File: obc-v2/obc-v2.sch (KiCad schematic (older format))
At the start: 19 parts

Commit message: obc-v2: Add voltage input and screw terminal
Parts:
- added J?: Screw_Terminal_01x02, symbol Connector:Screw_Terminal_01x02
- C? (x10): symbol Device:C -> obc-v2-rescue:C-Device
- FB?: symbol Device:Ferrite_Bead -> obc-v2-rescue:Ferrite_Bead-Device
- SW?: symbol Switch:SW_Push_Dual -> obc-v2-rescue:SW_Push_Dual-Switch
- U?: symbol MCU_Microchip_SAML_NEW:ATSAML10E16A-AF -> obc-v2-rescue:ATSAML10E16A-AF-MCU_Microchip_SAML_NEW
- U?: symbol Memory_EEPROM:AT25xxx -> obc-v2-rescue:AT25xxx-Memory_EEPROM
- U?: symbol Sensor_Pressure:MS5607-02BA -> obc-v2-rescue:MS5607-02BA-Sensor_Pressure
- U?: symbol Regulator_Linear:MIC5219-3.3YM5 -> obc-v2-rescue:MIC5219-3.3YM5-Regulator_Linear
- X?: symbol Oscillator:ASCO -> obc-v2-rescue:ASCO-Oscillator
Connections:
- net labels added: VIN
- wire segments 54 -> 55
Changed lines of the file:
@@
 RX
 $Comp
-L power:+3.3V #PWR?
+L obc-v2-rescue:+3.3V-power #PWR?
 U 1 1 61149F54
 P 2600 1150
@@
 $EndComp
 $Comp
-L Device:C C?
+L obc-v2-rescue:C-Device C?
 U 1 1 6114B5C3
 P 2300 1750
@@
 $EndComp
 $Comp
-L Device:C C?
+L obc-v2-rescue:C-Device C?
 U 1 1 6114F91D
 P 2300 2000
@@
 	2600 2000 2600 2250
 $Comp
-L power:GND #PWR?
+L obc-v2-rescue:GND-power #PWR?
 U 1 1 61151116
 P 1850 2000
@@
 $EndComp
 $Comp
-L Device:C C?
+L obc-v2-rescue:C-Device C?
 U 1 1 61151D34
 P 3550 2100
@@
 $EndComp
 $Comp
-L power:GND #PWR?
+L obc-v2-rescue:GND-power #PWR?
 U 1 1 611522C8
 P 3150 1550
@@
 $EndComp
 $Comp
-L Device:C C?
+L obc-v2-rescue:C-Device C?
 U 1 1 61159BEC
 P 3000 1700
@@
 $EndComp
 $Comp
-L power:GND #PWR?
+L obc-v2-rescue:GND-power #PWR?
 U 1 1 61107CFD
 P 2900 4350
@@
 $EndComp
 $Comp
-L Device:C C?
+L obc-v2-rescue:C-Device C?
 U 1 1 6115BCFD
 P 3000 1900
@@
 	2850 1700 2700 1700
 $Comp
-L Device:C C?
+L obc-v2-rescue:C-Device C?
 U 1 1 61165FAE
 P 3550 1150
@@
 	2150 1750 1850 1750
 $Comp
-L Oscillator:ASCO X?
+L obc-v2-rescue:ASCO-Oscillator X?
 U 1 1 611689B2
 P 5350 1350
@@
 $EndComp
 $Comp
-L power:GND #PWR?
+L obc-v2-rescue:GND-power #PWR?
 U 1 1 6116B41C
 P 5350 1650
@@
 $EndComp
 $Comp
-L power:+3.3V #PWR?
+L obc-v2-rescue:+3.3V-power #PWR?
 U 1 1 6116B9D5
 P 5350 1050
@@
 32-bit 32MHz ARM Processor
 $Comp
-L Memory_EEPROM:AT25xxx U?
+L obc-v2-rescue:AT25xxx-Memory_EEPROM U?
 U 1 1 61172006
 P 5500 2750
@@
 $EndComp
 $Comp
-L power:GND #PWR?
+L obc-v2-rescue:GND-power #PWR?
 U 1 1 611762E7
 P 5500 3050
@@
 $EndComp
 $Comp
-L power:+3.3V #PWR?
+L obc-v2-rescue:+3.3V-power #PWR?
 U 1 1 611767CC
 P 5500 2450
@@
 SCK
 $Comp
-L power:+3.3V #PWR?
+L obc-v2-rescue:+3.3V-power #PWR?
 U 1 1 611772E8
 P 5000 2650
@@
 4MB Flash Memory
 $Comp
-L Device:Ferrite_Bead FB?
+L obc-v2-rescue:Ferrite_Bead-Device FB?
 U 1 1 611AF1D7
 P 2600 1550
@@
 	3700 2100 3700 1150
 $Comp
-L power:GND #PWR?
+L obc-v2-rescue:GND-power #PWR?
 U 1 1 611FC866
 P 3700 1050
@@
 NoConn ~ 7450 3700
 $Comp
-L power:GND #PWR?
+L obc-v2-rescue:GND-power #PWR?
 U 1 1 612718CF
 P 7550 4200
@@
 	7850 4200 7950 4200
 $Comp
-L power:+3V3 #PWR?
+L obc-v2-rescue:+3V3-power #PWR?
 U 1 1 61272ED0
 P 7300 3600
@@
 INT4_GYRO
 $Comp
-L power:+3V3 #PWR?
+L obc-v2-rescue:+3V3-power #PWR?
 U 1 1 61277D25
 P 7600 2550
@@
 $EndComp
 $Comp
-L power:+3V3 #PWR?
+L obc-v2-rescue:+3V3-power #PWR?
 U 1 1 612781FE
 P 8100 2550
@@
 $EndComp
 $Comp
-L Device:C C?
+L obc-v2-rescue:C-Device C?
 U 1 1 612799A4
 P 7600 2700
@@
 $EndComp
 $Comp
-L Device:C C?
+L obc-v2-rescue:C-Device C?
 U 1 1 6127A006
 P 8100 2700
@@
 $EndComp
 $Comp
-L power:GND #PWR?
+L obc-v2-rescue:GND-power #PWR?
 U 1 1 6127AE14
 P 7600 2850
@@
 $EndComp
 $Comp
-L power:GND #PWR?
+L obc-v2-rescue:GND-power #PWR?
 U 1 1 6127B677
 P 8100 2850
@@
 INT4_GYRO
 $Comp
-L MCU_Microchip_SAML_NEW:ATSAML10E16A-AF U?
+L obc-v2-rescue:ATSAML10E16A-AF-MCU_Microchip_SAML_NEW U?
 U 1 1 61106D2F
 P 2750 3250
@@
 	6900 2250 9050 2250
 $Comp
-L Sensor_Pressure:MS5607-02BA U?
+L obc-v2-rescue:MS5607-02BA-Sensor_Pressure U?
 U 1 1 61291CE6
 P 9100 1400
@@
 $EndComp
 $Comp
-L power:GND #PWR?
+L obc-v2-rescue:GND-power #PWR?
 U 1 1 61292644
 P 9100 1800
@@
 $EndComp
 $Comp
-L power:+3V3 #PWR?
+L obc-v2-rescue:+3V3-power #PWR?
 U 1 1 61292BCA
 P 9100 1000
@@
 $EndComp
 $Comp
-L power:GND #PWR?
+L obc-v2-rescue:GND-power #PWR?
 U 1 1 6129E849
 P 5400 4700
@@
 $EndComp
 $Comp
-L power:+3V3 #PWR?
+L obc-v2-rescue:+3V3-power #PWR?
 U 1 1 6129EE3F
 P 5400 4050
@@
 1-wire Interface
 $Comp
-L Switch:SW_Push_Dual SW?
+L obc-v2-rescue:SW_Push_Dual-Switch SW?
 U 1 1 612A144F
 P 1600 1150
@@
 RESET*
 $Comp
-L power:GND #PWR?
+L obc-v2-rescue:GND-power #PWR?
 U 1 1 61309369
 P 1400 1350
@@
 	1800 1150 1800 1350
 $Comp
-L Regulator_Linear:MIC5219-3.3YM5 U?
+L obc-v2-rescue:MIC5219-3.3YM5-Regulator_Linear U?
 U 1 1 6130CF2C
 P 3000 5500
@@
 $EndComp
 $Comp
-L power:GND #PWR?
+L obc-v2-rescue:GND-power #PWR?
 U 1 1 6130E43E
 P 3000 5800
@@
 $EndComp
 $Comp
-L power:+3V3 #PWR?
+L obc-v2-rescue:+3V3-power #PWR?
 U 1 1 6130EAA8
 P 3750 5400
@@
 $EndComp
 $Comp
-L Device:C C?
+L obc-v2-rescue:C-Device C?
 U 1 1 6130FC01
 P 3450 5250
@@
 	3300 5400 3450 5400
 $Comp
-L power:GND #PWR?
+L obc-v2-rescue:GND-power #PWR?
 U 1 1 61312359
 P 3450 5100
@@
 Connection ~ 3450 5400
 $Comp
-L Device:C C?
+L obc-v2-rescue:C-Device C?
 U 1 1 61313A92
 P 3450 5650
@@
 $EndComp
 $Comp
-L power:GND #PWR?
+L obc-v2-rescue:GND-power #PWR?
 U 1 1 613140DB
 P 3450 5800
@@
 	3300 5500 3450 5500
 Wire Notes Line
-	2250 4850 4100 4850
-Wire Notes Line
 	4100 4850 4100 6200
 Wire Notes Line
-	4100 6200 2250 6200
-Wire Notes Line
-	2250 6200 2250 4850
+	1750 6200 1750 4850
 Text Notes 2300 6150 0    50   ~ 0
 Voltage Regulator
+$Comp
+L Connector:Screw_Terminal_01x02 J?
+U 1 1 61396620
+P 1950 5550
+F 0 "J?" H 1900 5650 50  0000 L CNN
+F 1 "Screw_Terminal_01x02" V 2050 5100 50  0000 L CNN
+F 2 "" H 1950 5550 50  0001 C CNN
+F 3 "" H 1950 5550 50  0001 C CNN
+	1    1950 5550
+	-1   0    0    1
+$EndComp
+$Comp
+L obc-v2-rescue:GND-power #PWR?
+U 1 1 6139C9C7
+P 2150 5450
+F 0 "#PWR?" H 2150 5200 50  0001 C CNN
+F 1 "GND" V 2150 5250 50  0000 C CNN
+F 2 "" H 2150 5450 50  0001 C CNN
+F 3 "" H 2150 5450 50  0001 C CNN
+	1    2150 5450
+	0    -1   -1   0
+$EndComp
+Wire Notes Line
+	1750 4850 4100 4850
+Wire Notes Line
+	1750 6200 4100 6200
+Text GLabel 2150 5550 2    50   Input ~ 0
+VIN
+Text GLabel 2700 5400 0    50   Input ~ 0
+VIN
+Wire Wire Line
+	2700 5500 2700 5400
 $EndSCHEMATC

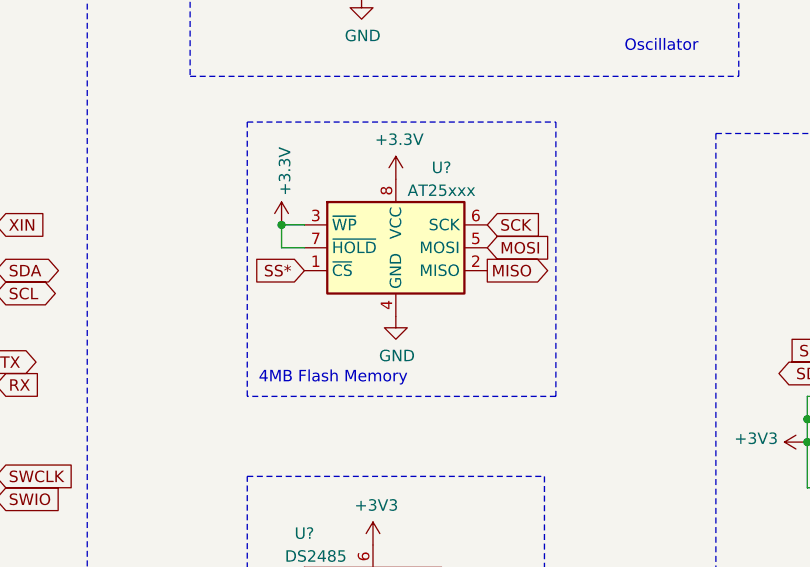
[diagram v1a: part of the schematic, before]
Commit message: obc-v2: Update 4MB flash chip to 1GB
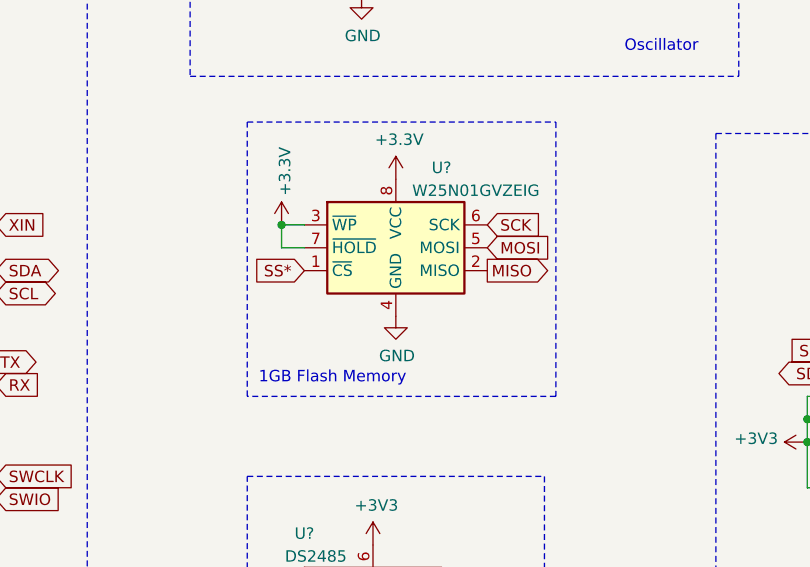
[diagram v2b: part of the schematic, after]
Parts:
- U?: value AT25xxx -> W25N01GVZEIG
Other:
- note added: "1GB Flash Memory"
- note removed: "4MB Flash Memory"
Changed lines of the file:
@@
 P 5500 2750
 F 0 "U?" H 5700 3100 50  0000 C CNN
-F 1 "AT25xxx" H 5700 3000 50  0000 C CNN
+F 1 "W25N01GVZEIG" H 5850 3000 50  0000 C CNN
 F 2 "" H 5500 2750 50  0001 C CNN
 F 3 "http://ww1.microchip.com/downloads/en/DeviceDoc/Atmel-8707-SEEPROM-AT25010B-020B-040B-Datasheet.pdf" H 5500 2750 50  0001 C CNN
@@
 	4850 3400 4850 2200
 Text Notes 4900 3350 0    50   ~ 0
-4MB Flash Memory
+1GB Flash Memory
 $Comp
 L obc-v2-rescue:Ferrite_Bead-Device FB?

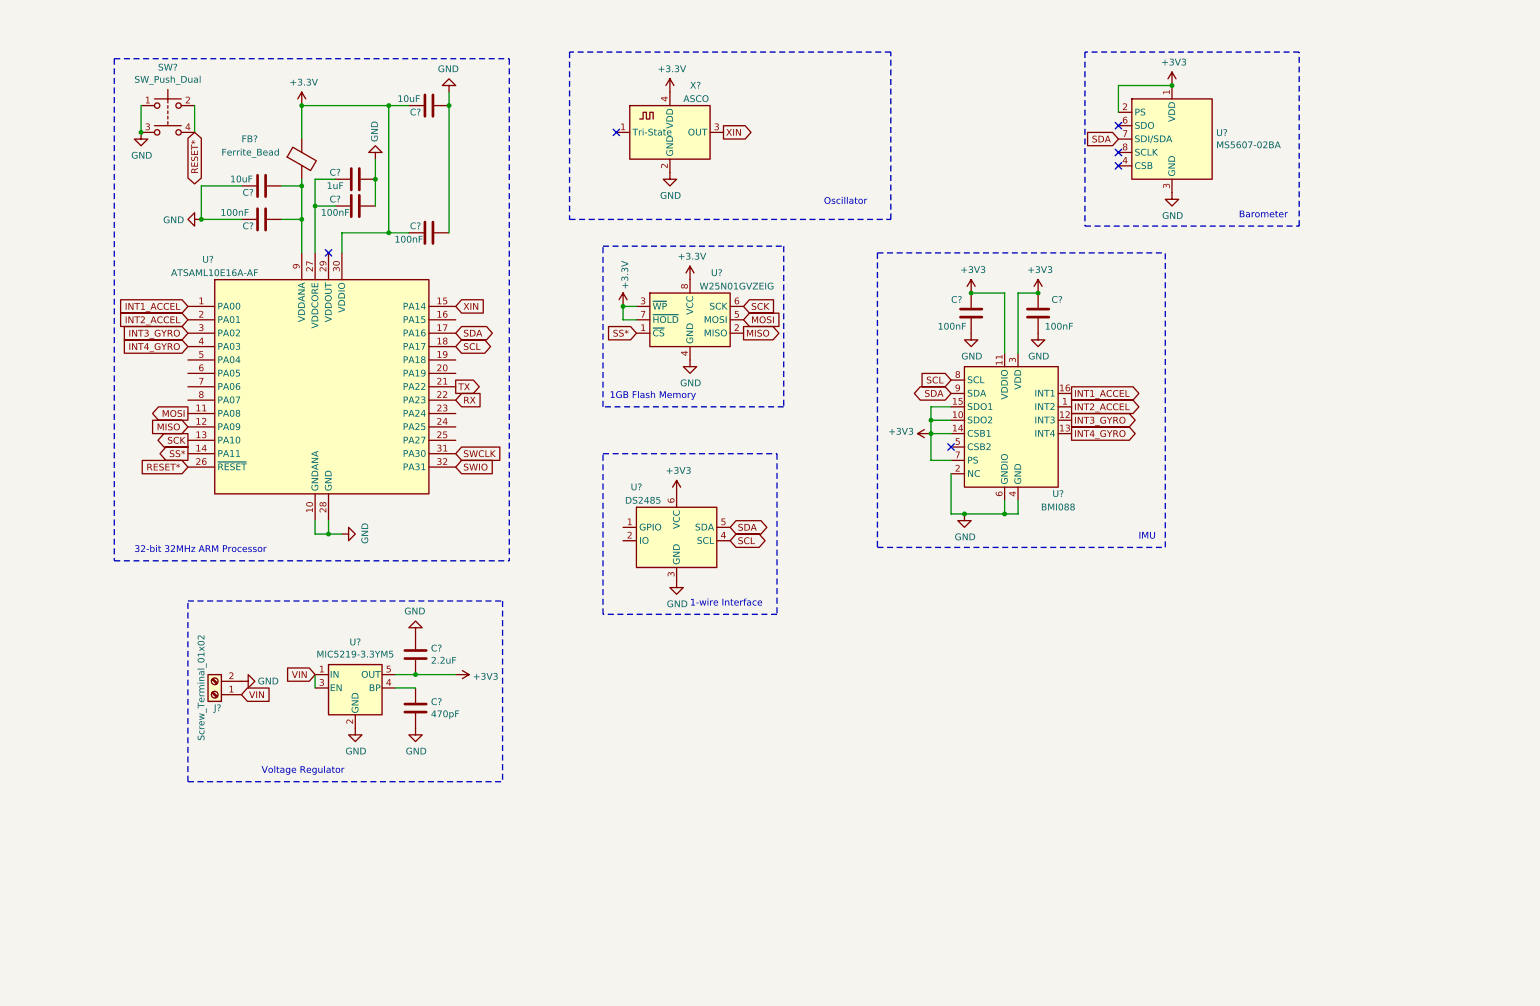
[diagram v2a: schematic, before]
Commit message: obc-v2: Add GPIO connector and LEDs
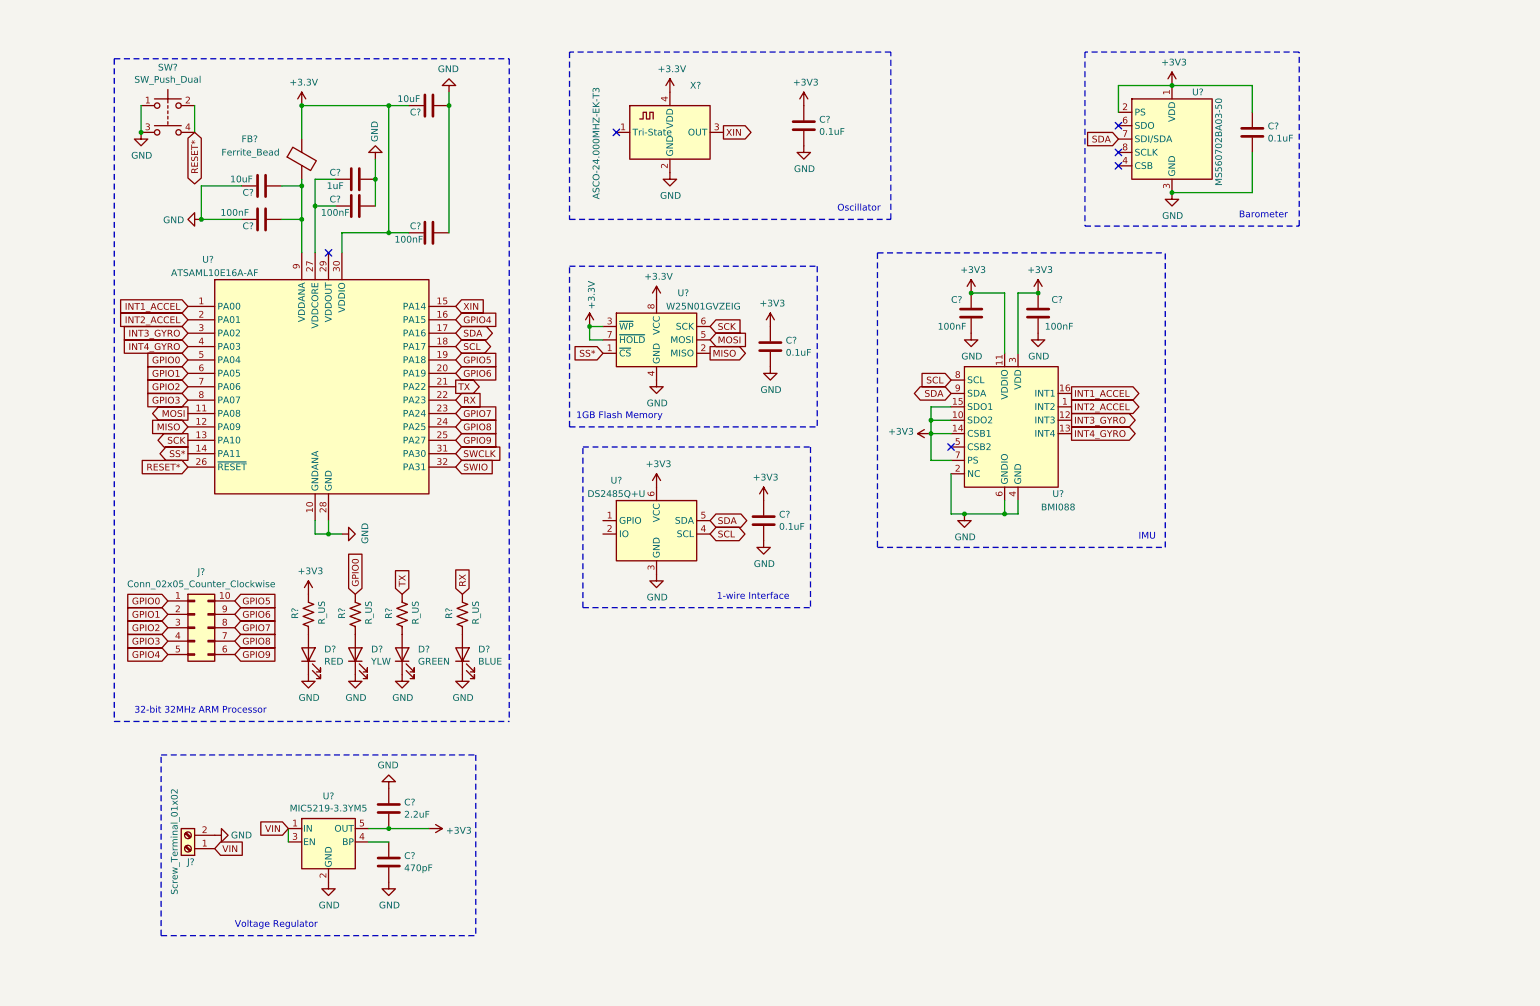
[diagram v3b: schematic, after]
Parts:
- added C? (x4): 0.1uF, symbol Device:C
- added D?: RED, symbol Device:LED
- added D?: YLW, symbol Device:LED
- added D?: GREEN, symbol Device:LED
- added D?: BLUE, symbol Device:LED
- added J?: Conn_02x05_Counter_Clockwise, symbol Connector_Generic:Conn_02x05_Counter_Clockwise
- added R? (x4): R_US, symbol Device:R_US
- U?: value MS5607-02BA -> MS560702BA03-50
- U?: value DS2485 -> DS2485Q+U
- X?: value ASCO -> ASCO-24.000MHZ-EK-T3
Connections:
- net +3V3: now also C?.1, C?.1, C?.1, C?.1, R?.2
- net GND: now also C?.2, C?.2, C?.2, C?.2, D?.1 (K), D?.1 (K), D?.1 (K), D?.1 (K)
- net RX: now also R?.2
- net TX: now also R?.2
- net GPIO4: now reaches U?.16 (PA15)
- net GPIO4: now also J?.5 (Pin_5)
- net GPIO5: now reaches U?.19 (PA18)
- net GPIO5: now also J?.10 (Pin_10)
- net GPIO6: now reaches U?.20 (PA19)
- net GPIO6: now also J?.9 (Pin_9)
- net GPIO7: now reaches U?.23 (PA24)
- net GPIO7: now also J?.8 (Pin_8)
- net GPIO8: now reaches U?.24 (PA25)
- net GPIO8: now also J?.7 (Pin_7)
- net GPIO9: now reaches U?.25 (PA27)
- net GPIO9: now also J?.6 (Pin_6)
- net GPIO0: now reaches U?.5 (PA04)
- net GPIO0: now also J?.1 (Pin_1), R?.2
- net GPIO1: now reaches U?.6 (PA05)
- net GPIO1: now also J?.2 (Pin_2)
- net GPIO2: now reaches U?.7 (PA06)
- net GPIO2: now also J?.3 (Pin_3)
- net GPIO3: now reaches U?.8 (PA07)
- net GPIO3: now also J?.4 (Pin_4)
- new net: D?.2 (A), R?.1 (x4)
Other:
- moved on the sheet: C?, J?, U?

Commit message: obc-v2: Fix reset button. Add debug header, RGB LED, and voltage divider circuit for measurement. Minor fixes to I2C bus, jumpers, and decoupling circuitry
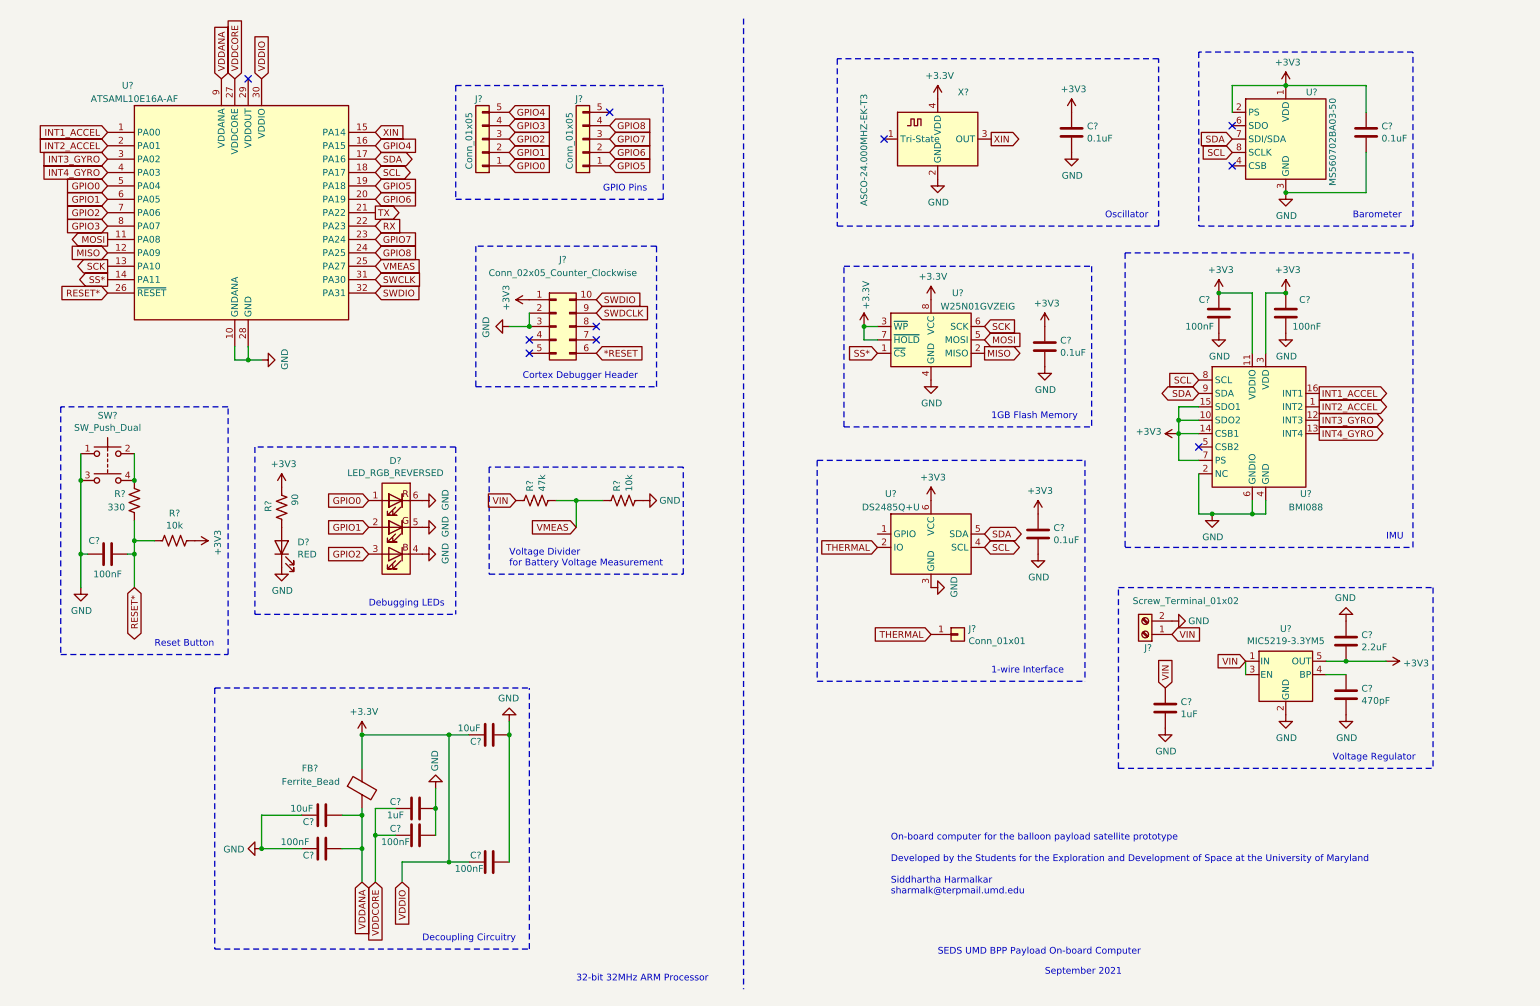
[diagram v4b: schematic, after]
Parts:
- removed D?: YLW, symbol Device:LED
- removed D?: GREEN, symbol Device:LED
- removed D?: BLUE, symbol Device:LED
- removed J?: Conn_02x05_Counter_Clockwise, symbol Connector_Generic:Conn_02x05_Counter_Clockwise
- removed R? (x3): R_US, symbol Device:R_US
- added C?: 100nF, symbol Device:C
- added C?: 1uF, symbol obc-v2-rescue:C-Device
- added D?: LED_RGB_REVERSED, symbol RGB_LED_REVERSED:LED_RGB_REVERSED
- added J? (x2): Conn_01x05, symbol Connector_Generic:Conn_01x05
- added J?: Conn_01x01, symbol Connector_Generic:Conn_01x01
- added J?: Conn_02x05_Counter_Clockwise, symbol Connector_Generic:Conn_02x05_Counter_Clockwise
- added R? (x2): 10k, symbol Device:R_US
- added R?: 330, symbol Device:R_US
- added R?: 47k, symbol Device:R_US
- R?: value R_US -> 90
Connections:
- net +3V3: now also J?.1 (Pin_1), R?.1
- net GND: now also C?.2, C?.2, D?.4 (BA), D?.5 (GA), D?.6 (RA), J?.2 (Pin_2), J?.3 (Pin_3), R?.2
- net GPIO0: now also D?.1 (RK), J?.1 (Pin_1)
- net GPIO1: now also D?.2 (GK), J?.2 (Pin_2)
- net GPIO2: now also D?.3 (BK), J?.3 (Pin_3)
- net GPIO3: now also J?.4 (Pin_4)
- net GPIO4: now also J?.5 (Pin_5)
- net GPIO5: now also J?.1 (Pin_1)
- net GPIO6: now also J?.2 (Pin_2)
- net GPIO7: now also J?.3 (Pin_3)
- net GPIO8: now also J?.4 (Pin_4)
- net RESET*: now also C?.1, R?.2, R?.2; no longer SW?.2, SW?.4
- net SCL: now also U?.8 (SCLK)
- net VIN: now also C?.1, R?.1
- net VDDCORE: now reaches C?.1, C?.1, U?.27 (VDDCORE)
- net VDDANA: now reaches C?.1, C?.2, FB?.2, U?.9 (VDDANA)
- net THERMAL: now reaches U?.2 (IO)
- net THERMAL: now also J?.1 (Pin_1)
- net GPIO9 renamed VMEAS
- net VMEAS: now also R?.1, R?.2
- net SWIO renamed SWDIO
- net SWDIO: now also J?.10 (Pin_10)
- new net: R?.1, SW?.2, SW?.4
- new net *RESET: J?.6 (Pin_6)
- new net SWDCLK: J?.9 (Pin_9)
- no-connect marks 6 -> 10
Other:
- note added: "Cortex Debugger Header"
- note added: "Debugging LEDs"
- note added: "Decoupling Circuitry"
- note added: "GPIO Pins"
- note added: "On-board computer for the balloon payload satellite prototype\n\nDeveloped by the Students for the Exploration and Development of Space at the University of Maryland\n\nSiddhartha Harmalkar\nsharmalk@terpmail.umd.edu"
- note added: "Reset Button"
- note added: "SEDS UMD BPP Payload On-board Computer"
- note added: "September 2021"
- note added: "Voltage Divider\nfor Battery Voltage Measurement"
- moved on the sheet: C?, D?, FB?, J?, R?, SW?, U?, X?
